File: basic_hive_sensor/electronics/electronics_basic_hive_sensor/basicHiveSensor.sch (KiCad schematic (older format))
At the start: 24 parts, among them J1 RJ45_Shielded, J2 RJ45_Shielded, J3 Conn_01x04_Male, J4 Conn_01x04_Male, J5 Conn_01x04_Male, J6 Conn_01x03_Male, J7 Conn_01x03_Male, J8 Conn_01x06_Male, SW1 SW_Push_45deg, SW2 SW_Push_45deg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

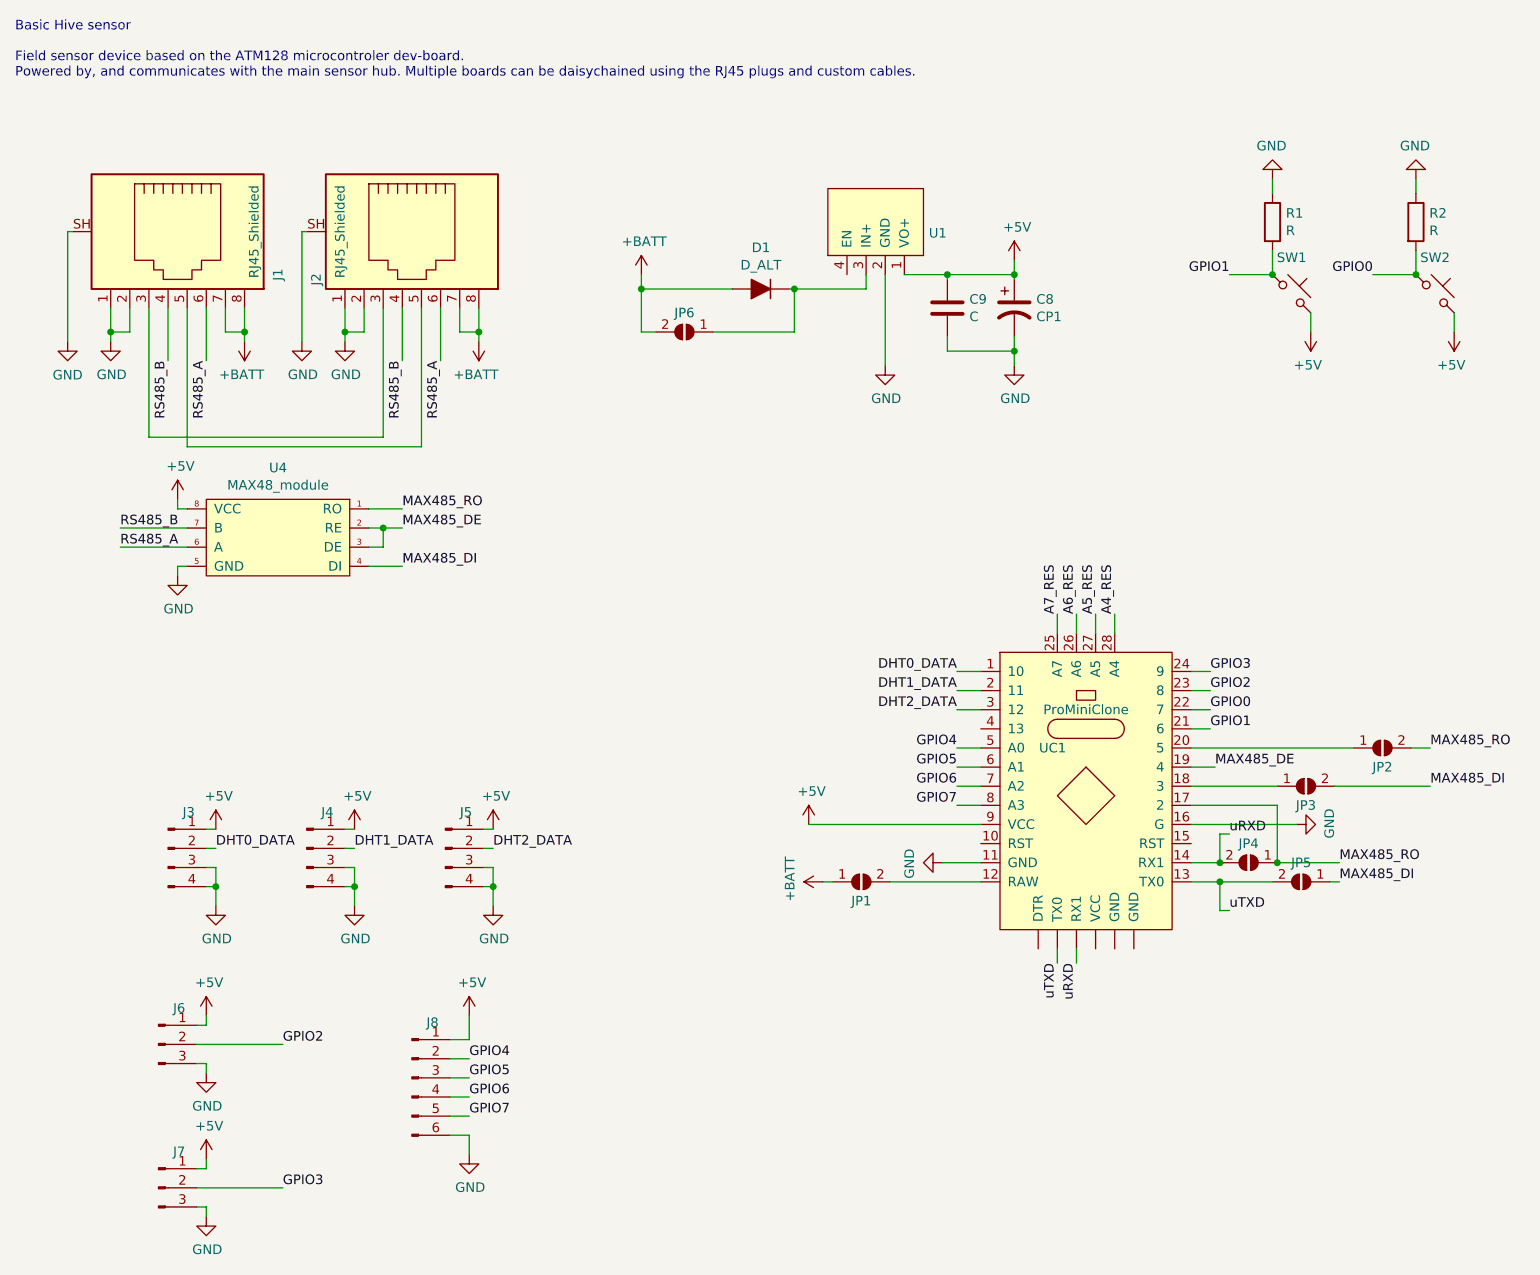
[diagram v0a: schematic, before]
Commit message: started working on GNSS time and NTP functionality, ESP32 timekeeping works, just need to update it from modem. need to parse the GNSS status for string. Played around with chatGPT, and got a fairly good solution for converting datetimeString to unix time. @TODO: the SIM7000 class makes little sense, needs a refactoring. I have functions for geting CSQ and GNSS data from modem in a totally different class.
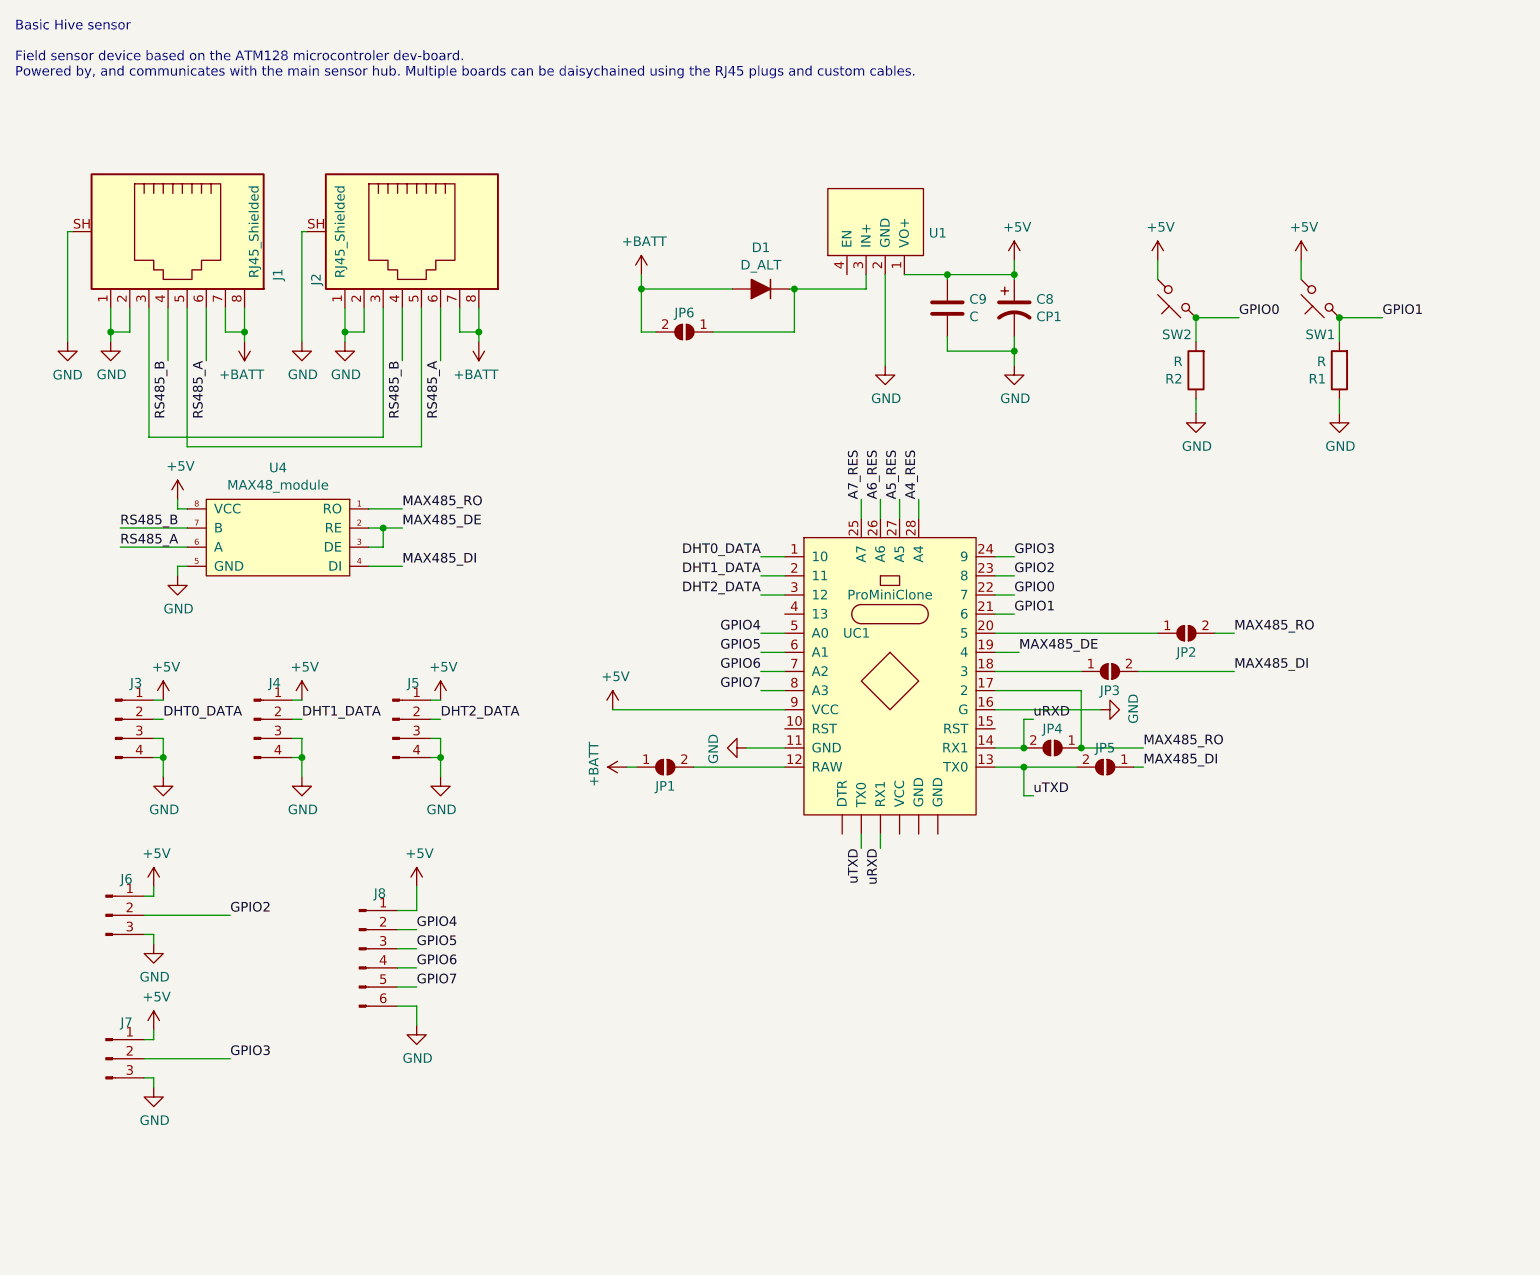
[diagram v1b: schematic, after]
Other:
- moved on the sheet: J3, J4, J5, J6, J7, J8, JP1, JP2, JP3, JP4, JP5, R1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
